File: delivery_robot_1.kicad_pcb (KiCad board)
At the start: 4 copper layers, 100 x 100 mm, 105 parts, among them J1 SWD, J10 Port C/D breakout, J13 Pi 5 UART, J14 Pi 5 power, J15 Motor2 encoder, J16 MDD20A PWM2/DIR2/GND, J2 XT30PW-M, J4 BOOT0 jumper, J5 Power test points, J6 MDD20A PWM1/DIR1/GND, J7 Motor1 encoder, J8 Port A breakout, J9 Port B breakout, SW1 RESET, U1 STM32F091RCTx, U2 PTPSM63606RDLR, U3 TPS54202DDCR, U4 TPS7A8101DRBR, U5 PTPSM63606RDLR, U6 USBLC6-4SC6, U7 USBLC6-4SC6, Y3 8MHz

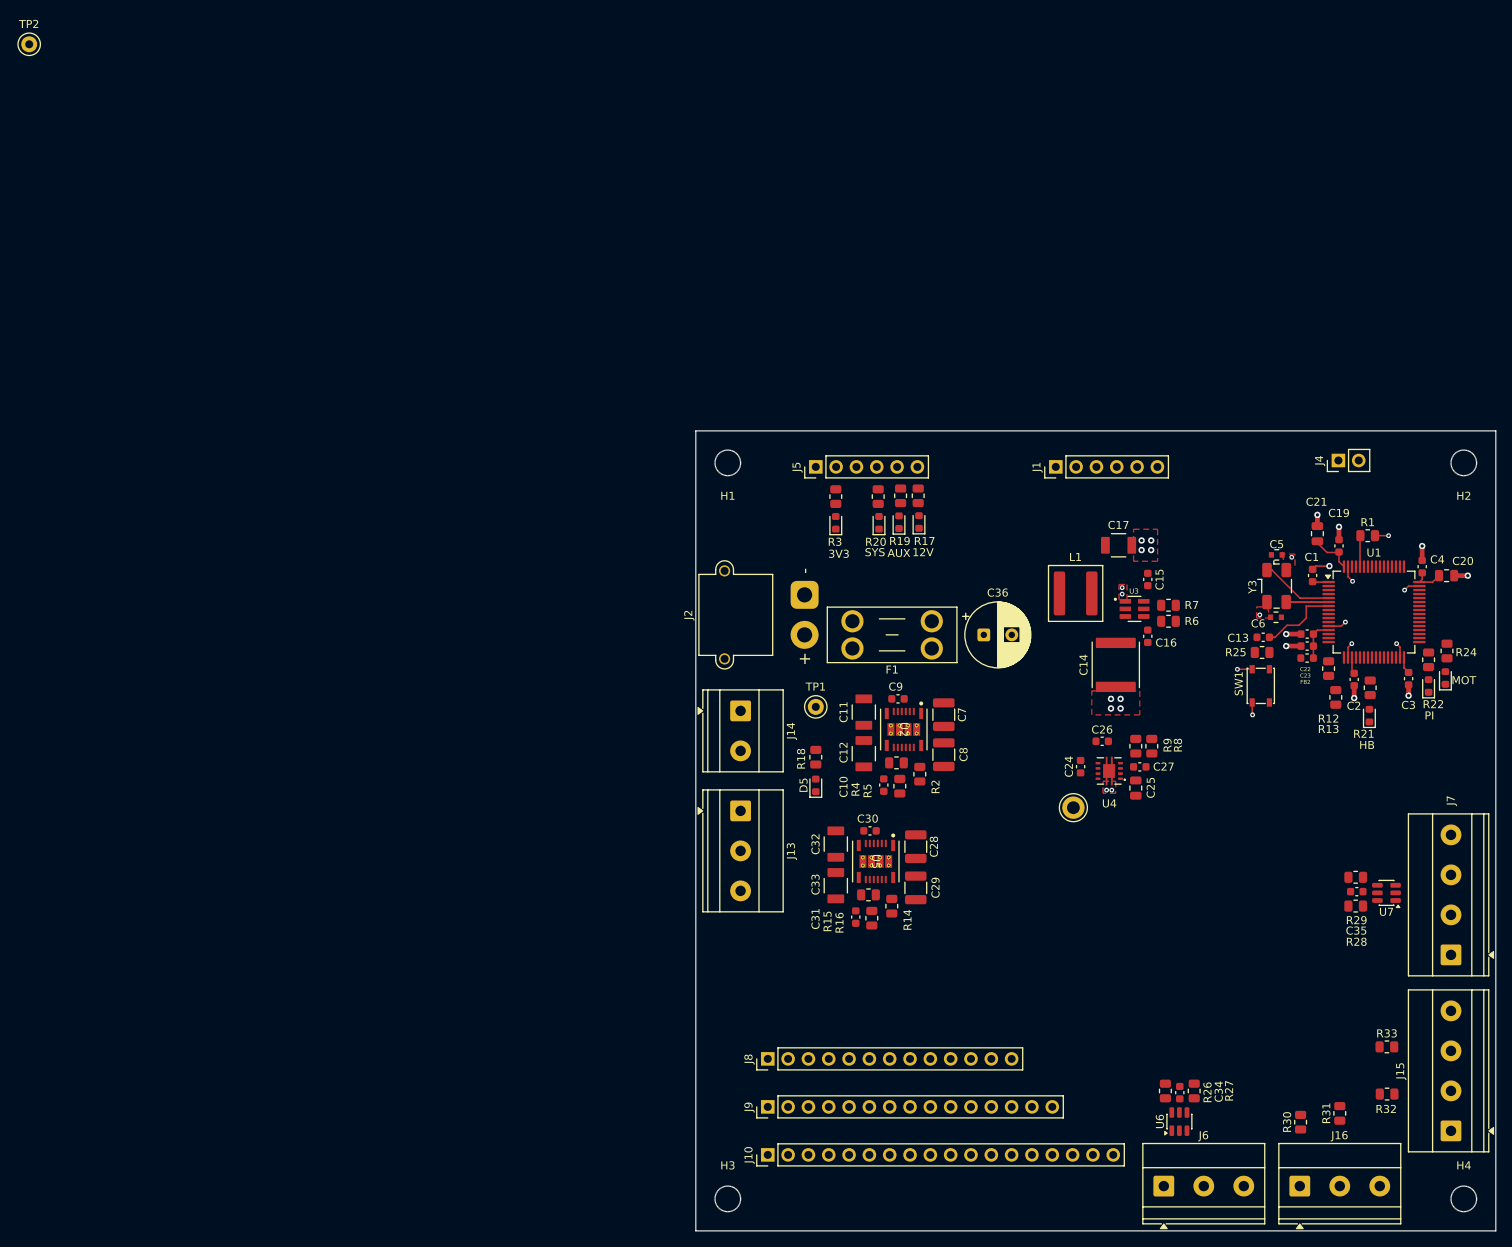
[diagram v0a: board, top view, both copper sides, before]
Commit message: Update the board from the schematic and place the new parts
As Update PCB from Schematic, on top of c692e23: 61 footprints added,
J8/J9/J13 swapped to their new footprints, U2/U5 refreshed from the
fixed library footprint, TP2 deleted, pad nets updated. Every existing
track and via is unchanged (87 items, identical), and Venya's latest
placement (LEDs, R12/R13, R26-R33, U6/U7, C34/C35, TP3) is kept.

Schematic parity: the seven LEDs renamed on the board (3V3, 12V, AUX,
SYS, HB, PI, MOT) get their schematic references back (D3, D4, D6, D7,
D8, D9, D11). Their rail names stay on the silkscreen as plain text in
the same spot, and the references move to the fab layer, so the board
looks the same and parity is clean.

Placement (rough; new parts next to the circuit they serve; small parts
placed clear of existing courtyards, pads and reference text):
- Input: C36 moves down beside the U2/U5 input caps; Q1 (drain tab
  facing F1), D12, R36 and D13 take its old spot right after F1.
- U3: C49 between U3 and C14, on the VIN/GND pins.
- Pi link: J13 (6-pin XH) in the same left-edge slot; J22/R43/C40/D15
  next to U5; Q2, R44-R46 and the VBAT sense divider below the MCU;
  R47 by J4.
- Servo: J17 on the top edge between J1 and J4, with F3 and D14 next to
  it; U8 and its resistors/caps in the free middle of the board.
- Encoders: U9/U10 with their RC caps next to R28/R29 and R32/R33;
  encoder-supply PTCs and DNP pull-ups beside them.
- Motor driver: R52/R53 pull-downs and F10/F11 by J6/J16.
- J8-J10 move up 12 mm; AUX ports J18-J21 and PTCs F4-F7 take the
  freed bottom-left edge.

Layout fixes:
- The In1 GND zone and all F.Cu GND zones use thermal reliefs on
  through-hole pads only (SMD pads stay solid; the U2/U5 thermal vias
  are forced solid).
- U2/U5 reference text off the pads, U3 reference 0.8 mm.
- Silkscreen: J14 +/-, J13-to-Pi pin map, SERVO, AUX port names, board
  name and revision.

DRC: 0 errors; 3 warnings (existing 0.5 mm FB2/C22/C23 references);
326 unrouted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
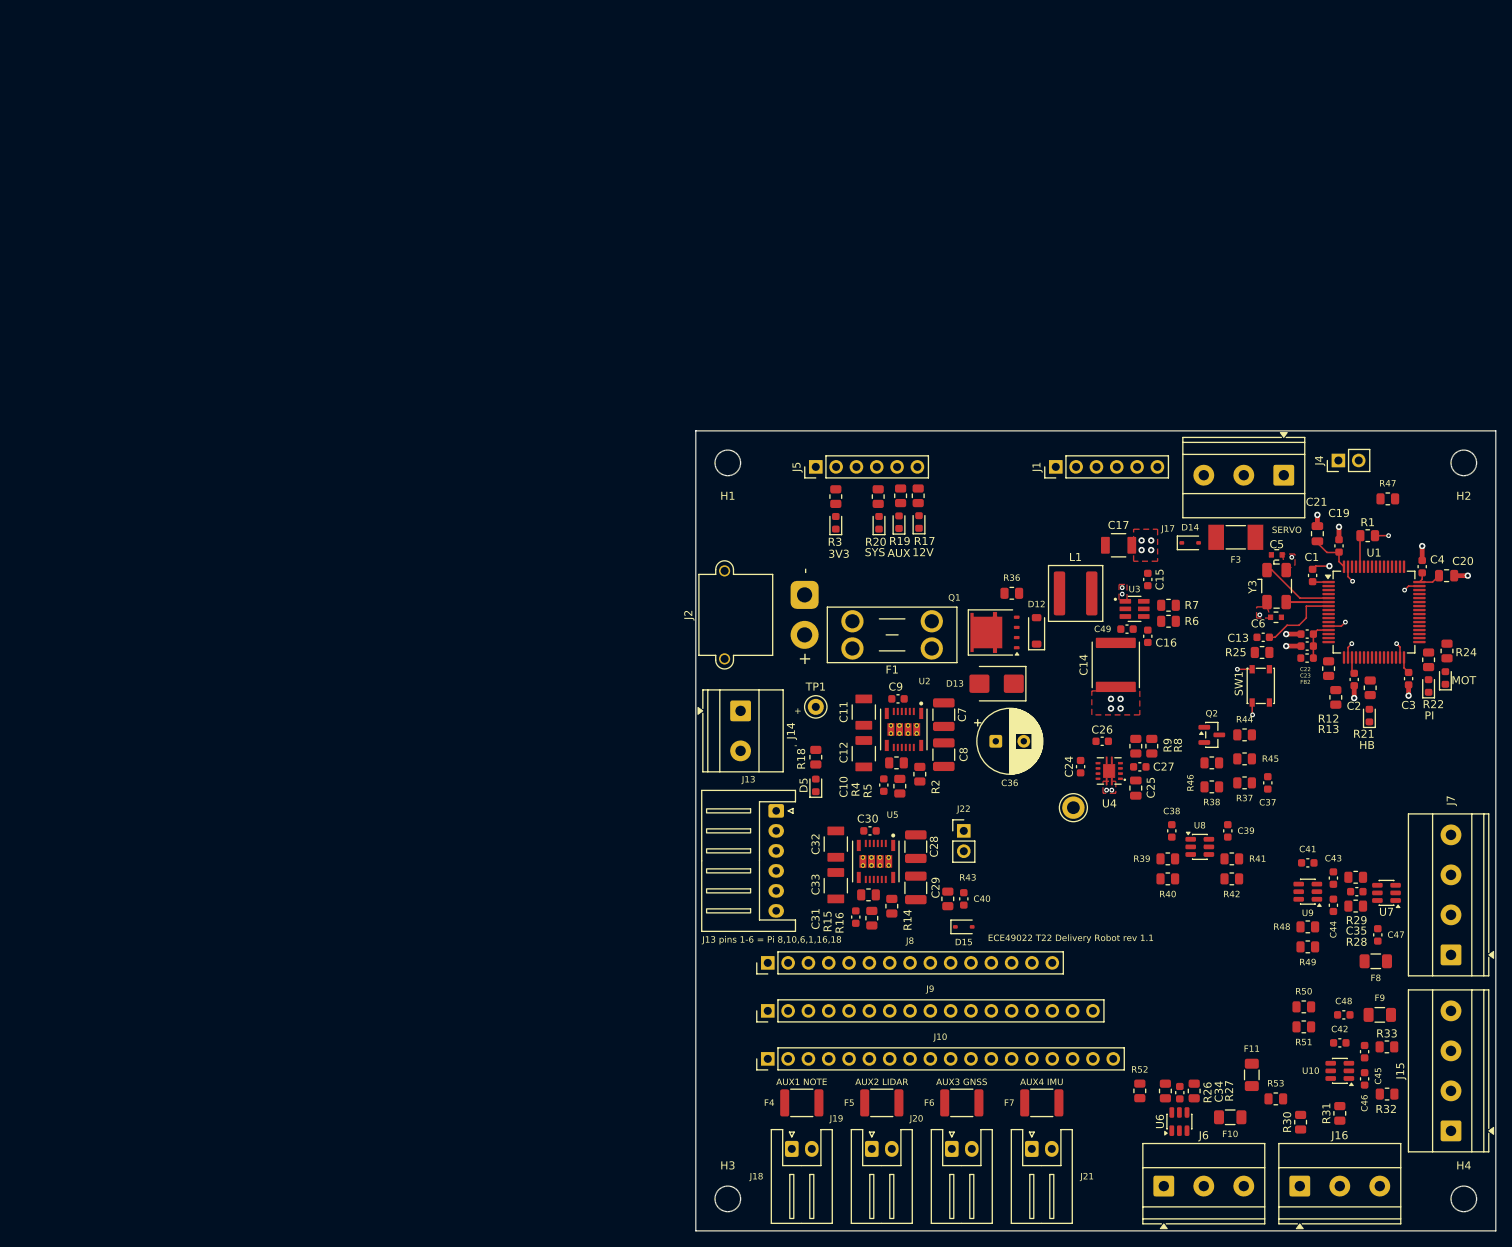
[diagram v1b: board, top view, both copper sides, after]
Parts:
- removed TP2: PI_5V, TestPoint:TestPoint_Keystone_5000-5004_Miniature
- added C37: 100nF / 50V X7R, Capacitor_SMD:C_0603_1608Metric, F.Cu at (156.5, 94.0)
- added C38: 100nF / 50V X7R, Capacitor_SMD:C_0603_1608Metric, F.Cu at (144.5, 100.0)
- added C39: 100nF / 50V X7R, Capacitor_SMD:C_0603_1608Metric, F.Cu at (151.5, 100.0)
- added C40: 1nF / 50V C0G, Capacitor_SMD:C_0603_1608Metric, F.Cu at (118.5, 108.5)
- added C41: 100nF / 50V X7R, Capacitor_SMD:C_0603_1608Metric, F.Cu at (161.5, 104.0)
- added C42: 100nF / 50V X7R, Capacitor_SMD:C_0603_1608Metric, F.Cu at (165.5, 126.5)
- added C43: 1nF / 50V C0G, Capacitor_SMD:C_0603_1608Metric, F.Cu at (164.7, 105.9)
- added C44: 1nF / 50V C0G, Capacitor_SMD:C_0603_1608Metric, F.Cu at (164.7, 109.3)
- added C45: 1nF / 50V C0G, Capacitor_SMD:C_0603_1608Metric, F.Cu at (168.6, 127.6)
- added C46: 1nF / 50V C0G, Capacitor_SMD:C_0603_1608Metric, F.Cu at (168.6, 131.0)
- added C47: 1uF / 16V X7R, Capacitor_SMD:C_0603_1608Metric, F.Cu at (170.2, 113.0)
- added C48: 1uF / 16V X7R, Capacitor_SMD:C_0603_1608Metric, F.Cu at (166.0, 123.0)
- added C49: 100nF / 50V X7R, Capacitor_SMD:C_0603_1608Metric, F.Cu at (138.9, 74.8)
- added D12: MMSZ5242B 12V, Diode_SMD:D_SOD-123, F.Cu at (127.6, 75.0)
- added D13: SMBJ16A, Diode_SMD:D_SMB, F.Cu at (122.6, 81.6)
- added D14: D5V0L1B2WS, Diode_SMD:D_SOD-323, F.Cu at (146.8, 64.0)
- added D15: BAT54WS, Diode_SMD:D_SOD-323, F.Cu at (118.5, 112.0)
- added F10: 0.2A hold, Fuse:Fuse_1206_3216Metric, F.Cu at (151.8, 135.8)
- added F11: 0.2A hold, Fuse:Fuse_1206_3216Metric, F.Cu at (154.5, 130.5)
- added F3: 5A fast, Fuse:Fuse_Littelfuse-NANO2-451_453, F.Cu at (152.5, 63.3)
- added F4: 1.5A hold, Fuse:Fuse_1812_4532Metric, F.Cu at (98.2, 134.0)
- added F5: 1.5A hold, Fuse:Fuse_1812_4532Metric, F.Cu at (108.2, 134.0)
- added F6: 1.5A hold, Fuse:Fuse_1812_4532Metric, F.Cu at (118.2, 134.0)
- added F7: 1.5A hold, Fuse:Fuse_1812_4532Metric, F.Cu at (128.2, 134.0)
- added F8: 0.2A hold, Fuse:Fuse_1206_3216Metric, F.Cu at (170.0, 116.3)
- added F9: 0.2A hold, Fuse:Fuse_1206_3216Metric, F.Cu at (170.5, 123.0)
- added J17: Latch servo, TerminalBlock_Phoenix:TerminalBlock_Phoenix_MKDS-1,5-3_1x03_P5.00mm_Horizontal, F.Cu at (158.5, 55.5)
- added J18: AUX1 Notecard, Connector_JST:JST_XH_S2B-XH-A_1x02_P2.50mm_Horizontal, F.Cu at (97.0, 139.8)
- added J19: AUX2 LiDAR, Connector_JST:JST_XH_S2B-XH-A_1x02_P2.50mm_Horizontal, F.Cu at (107.0, 139.8)
- added J20: AUX3 GNSS, Connector_JST:JST_XH_S2B-XH-A_1x02_P2.50mm_Horizontal, F.Cu at (117.0, 139.8)
- added J21: AUX4 IMU, Connector_JST:JST_XH_S2B-XH-A_1x02_P2.50mm_Horizontal, F.Cu at (127.0, 139.8)
- added J22: AUX force-on, Connector_PinHeader_2.54mm:PinHeader_1x02_P2.54mm_Vertical, F.Cu at (118.5, 100.0)
- added Q1: SQJ409EP, Package_SO:PowerPAK_SO-8L_Single, F.Cu at (122.4, 75.2)
- added Q2: DMN63D8L, Package_TO_SOT_SMD:SOT-23, F.Cu at (149.5, 88.0)
- added R36: 10k, Resistor_SMD:R_0805_2012Metric, F.Cu at (124.5, 70.3)
- added R37: 100k, Resistor_SMD:R_0805_2012Metric, F.Cu at (153.6, 94.0)
- added R38: 22.1k, Resistor_SMD:R_0805_2012Metric, F.Cu at (149.5, 94.5)
- added R39: 10k, Resistor_SMD:R_0805_2012Metric, F.Cu at (144.0, 103.5)
- added R40: 10k, Resistor_SMD:R_0805_2012Metric, F.Cu at (144.0, 106.0)
- added R41: 10k, Resistor_SMD:R_0805_2012Metric, F.Cu at (152.0, 103.5)
- added R42: 100, Resistor_SMD:R_0805_2012Metric, F.Cu at (152.0, 106.0)
- added R43: 100k, Resistor_SMD:R_0805_2012Metric, F.Cu at (116.5, 108.5)
- added R44: 10k, Resistor_SMD:R_0805_2012Metric, F.Cu at (153.6, 88.0)
- added R45: 100k, Resistor_SMD:R_0805_2012Metric, F.Cu at (153.6, 91.0)
- added R46: 100k, Resistor_SMD:R_0805_2012Metric, F.Cu at (149.5, 91.5)
- added R47: 1k, Resistor_SMD:R_0805_2012Metric, F.Cu at (171.5, 58.5)
- added R48: 4.7k, Resistor_SMD:R_0805_2012Metric, F.Cu at (161.5, 112.0)
- added R49: 4.7k, Resistor_SMD:R_0805_2012Metric, F.Cu at (161.5, 114.5)
- added R50: 4.7k, Resistor_SMD:R_0805_2012Metric, F.Cu at (161.0, 122.0)
- added R51: 4.7k, Resistor_SMD:R_0805_2012Metric, F.Cu at (161.0, 124.5)
- added R52: 10k, Resistor_SMD:R_0805_2012Metric, F.Cu at (140.5, 132.5)
- added R53: 10k, Resistor_SMD:R_0805_2012Metric, F.Cu at (157.5, 133.5)
- added U10: 74LVC2G17, Package_TO_SOT_SMD:SOT-23-6, F.Cu at (165.5, 130.0)
- added U8: SN74LVC1T45DBV, Package_TO_SOT_SMD:SOT-23-6, F.Cu at (148.0, 102.0)
- added U9: 74LVC2G17, Package_TO_SOT_SMD:SOT-23-6, F.Cu at (161.5, 107.6)
- C26, C27: value 470nF / 16V X7R -> 10nF / 100V X7R
- F1: value 7.5A / 32VDC -> 10A / 32VDC
- J13: value Pi 5 UART -> Pi 5 link; footprint TerminalBlock_Phoenix:TerminalBlock_Phoenix_MKDS-1,5-3_1x03_P5.00mm_Horizontal -> Connector_JST:JST_XH_S6B-XH-A_1x06_P2.50mm_Horizontal
- J8: footprint Connector_PinHeader_2.54mm:PinHeader_1x13_P2.54mm_Vertical -> Connector_PinHeader_2.54mm:PinHeader_1x15_P2.54mm_Vertical
- J9: footprint Connector_PinHeader_2.54mm:PinHeader_1x15_P2.54mm_Vertical -> Connector_PinHeader_2.54mm:PinHeader_1x17_P2.54mm_Vertical
- R12, R13, R28, R29, R32, R33: value 100 -> 1k
- U2, U5: value PTPSM63606RDLR -> TPSM63606RDLR
- moved C36 13.4 mm to (122.5, 88.8)
- moved J10 12.0 mm to (94.0, 128.5)
- moved J8 12.0 mm to (94.0, 116.5)
- moved J9 12.0 mm to (94.0, 122.5)
- moved J13 4.45 mm to (95.0, 97.5)
- renumbered MOT to D11, 3V3 to D3, 12V to D4, AUX to D6, SYS to D7, HB to D8, PI to D9
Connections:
- net Net-(J2-Pin_2) renamed VBAT_IN
- net PA0 renamed VBAT_SENSE
- net PA1 renamed PI_3V3_SENSE
- F1 pad 1: +12V -> VBAT_FUSED
- J15 pad 1: +5V_SYS -> /Motor Control/ENC2_5V
- J15 pad 2: /Motor Control/ENC2_A_CONN -> GND
- J15 pad 3: /Motor Control/ENC2_B_CONN -> /Motor Control/ENC2_A_CONN
- J15 pad 4: GND -> /Motor Control/ENC2_B_CONN
- J16 pad 3: GND -> /Motor Control/M2_DRV_GND
- J5 pad 1: GND -> +12V
- J5 pad 2: +3V3 -> GND
- J5 pad 3: +3.3VA -> +5V_AUX
- J5 pad 5: +5V_AUX -> +3V3
- J5 pad 6: +12V -> +3.3VA
- J6 pad 3: GND -> /Motor Control/M1_DRV_GND
- J7 pad 1: +5V_SYS -> /Motor Control/ENC1_5V
- J7 pad 2: /Motor Control/ENC1_A_CONN -> GND
- J7 pad 3: /Motor Control/ENC1_B_CONN -> /Motor Control/ENC1_A_CONN
- J7 pad 4: GND -> /Motor Control/ENC1_B_CONN
- J8 pad 10: PA10 -> ENC2_B
- J8 pad 11: PA11 -> PA10
- J8 pad 12: PA12 -> PA11
- J8 pad 13: GND -> PA12
- J8 pad 7: MOTOR2_PWM -> MOTOR1_PWM
- J8 pad 8: ENC2_A -> MOTOR2_PWM
- J8 pad 9: ENC2_B -> ENC2_A
- J9 pad 1: PB1 -> MOTOR1_DIR
- J9 pad 10: PB11 -> PB9
- J9 pad 11: LED_PI_LINK -> SERVO_TX
- J9 pad 12: PB13 -> SERVO_DIR
- J9 pad 13: LED_MOTOR -> LED_PI_LINK
- J9 pad 14: PB15 -> PB13
- J9 pad 15: GND -> LED_MOTOR
- J9 pad 2: MOTOR2_DIR -> PB1
- J9 pad 3: PB4 -> MOTOR2_DIR
- J9 pad 4: PB5 -> ENC1_B
- J9 pad 5: PB6 -> PB4
- J9 pad 6: PB7 -> PB5
- J9 pad 7: PB8 -> PB6
- J9 pad 8: PB9 -> PB7
- J9 pad 9: PB10 -> PB8
- R28 pad 1: ENC1_A -> /Motor Control/ENC1_A_F
- R29 pad 1: ENC1_B -> /Motor Control/ENC1_B_F
- R32 pad 1: ENC2_A -> /Motor Control/ENC2_A_F
- R33 pad 1: ENC2_B -> /Motor Control/ENC2_B_F
- U1 pad 29: PB10 -> SERVO_TX
- U1 pad 30: PB11 -> SERVO_DIR
- U5 pad 14: +12V -> AUX_EN
- U6 pad 4: unconnected-(U6-I/O3-Pad4) -> /Motor Control/MOTOR2_PWM_CONN
- U6 pad 6: unconnected-(U6-I/O4-Pad6) -> /Motor Control/MOTOR2_DIR_CONN
- U7 pad 4: unconnected-(U7-I/O3-Pad4) -> /Motor Control/ENC2_A_CONN
- U7 pad 6: unconnected-(U7-I/O4-Pad6) -> /Motor Control/ENC2_B_CONN
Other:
- board text added: "+"
- board text added: "-"
- board text added: "12V"
- board text added: "3V3"
- board text added: "AUX"
- board text added: "AUX1 NOTE"
- board text added: "AUX2 LIDAR"
- board text added: "AUX3 GNSS"
- board text added: "AUX4 IMU"
- board text added: "ECE49022 T22 Delivery Robot rev 1.1"
- board text added: "HB"
- board text added: "J13 pins 1-6 = Pi 8,10,6,1,16,18"
- board text added: "MOT"
- board text added: "PI"
- board text added: "SERVO"
- board text added: "SYS"
